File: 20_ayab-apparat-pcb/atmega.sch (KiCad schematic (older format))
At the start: 35 parts, among them P7 CONN_3X2, P8 CONN_4, P9 CONN_2, SW1 SW_PUSH, U6 ATMEGA32U4-A, X1 16MHz, X2 USBMINI

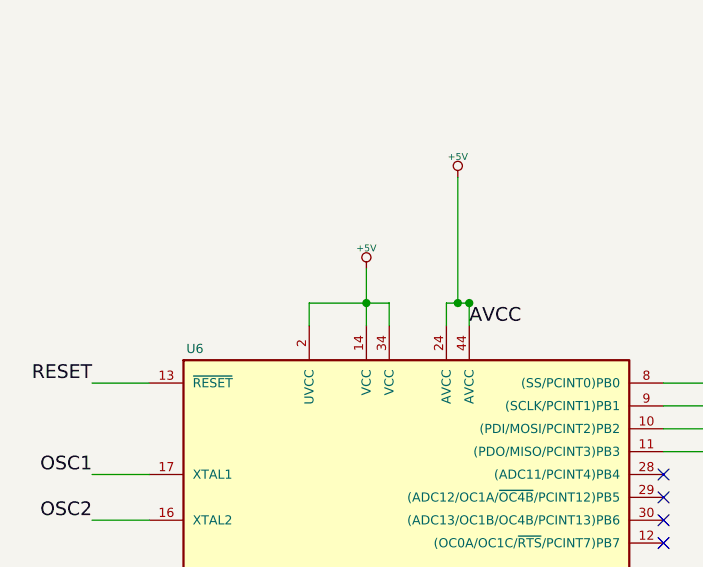
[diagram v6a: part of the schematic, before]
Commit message: Changed power supply of ATMega to VUSB finished BOM CSV -> ready to layout
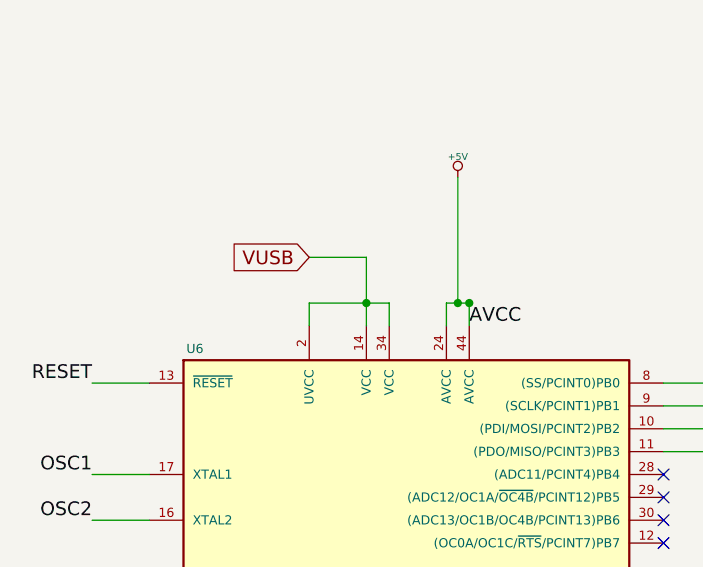
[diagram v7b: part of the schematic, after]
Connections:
- net +5V: no longer U6.14 (VCC), U6.2 (UVCC), U6.34 (VCC)
- net VUSB: now also U6.14 (VCC), U6.2 (UVCC), U6.34 (VCC)
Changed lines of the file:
@@
 $EndComp
 $Comp
-L +5V #PWR037
-U 1 1 52E8098A
-P 2650 2450
-F 0 "#PWR037" H 2650 2540 20  0001 C CNN
-F 1 "+5V" H 2650 2540 30  0000 C CNN
-F 2 "" H 2650 2450 60  0000 C CNN
-F 3 "" H 2650 2450 60  0000 C CNN
-	1    2650 2450
-	1    0    0    -1
-$EndComp
-$Comp
-L PWR_FLAG #FLG038
+L PWR_FLAG #FLG037
 U 1 1 52E809A6
 P 9200 1150
-F 0 "#FLG038" H 9200 1245 30  0001 C CNN
+F 0 "#FLG037" H 9200 1245 30  0001 C CNN
 F 1 "PWR_FLAG" H 9200 1330 30  0000 C CNN
 F 2 "" H 9200 1150 60  0000 C CNN
@@
 $EndComp
 $Comp
-L GND #PWR039
+L GND #PWR038
 U 1 1 52E80AA1
 P 1450 5850
-F 0 "#PWR039" H 1450 5850 30  0001 C CNN
+F 0 "#PWR038" H 1450 5850 30  0001 C CNN
 F 1 "GND" H 1450 5780 30  0001 C CNN
 F 2 "" H 1450 5850 60  0000 C CNN
@@
 ISP
 $Comp
-L GND #PWR040
+L GND #PWR039
 U 1 1 52E80DFA
 P 7100 5850
-F 0 "#PWR040" H 7100 5850 30  0001 C CNN
+F 0 "#PWR039" H 7100 5850 30  0001 C CNN
 F 1 "GND" H 7100 5780 30  0001 C CNN
 F 2 "" H 7100 5850 60  0000 C CNN
@@
 MOSI
 $Comp
-L +5V #PWR041
+L +5V #PWR040
 U 1 1 52E80E45
 P 7100 5600
-F 0 "#PWR041" H 7100 5690 20  0001 C CNN
+F 0 "#PWR040" H 7100 5690 20  0001 C CNN
 F 1 "+5V" H 7100 5690 30  0000 C CNN
 F 2 "" H 7100 5600 60  0000 C CNN
@@
 $EndComp
 $Comp
-L GND #PWR042
+L GND #PWR041
 U 1 1 52E813A7
 P 6750 1800
-F 0 "#PWR042" H 6750 1800 30  0001 C CNN
+F 0 "#PWR041" H 6750 1800 30  0001 C CNN
 F 1 "GND" H 6750 1730 30  0001 C CNN
 F 2 "" H 6750 1800 60  0000 C CNN
@@
 $EndComp
 $Comp
-L +5V #PWR043
+L +5V #PWR042
 U 1 1 52E81906
 P 4350 3500
-F 0 "#PWR043" H 4350 3590 20  0001 C CNN
+F 0 "#PWR042" H 4350 3590 20  0001 C CNN
 F 1 "+5V" H 4350 3590 30  0000 C CNN
 F 2 "" H 4350 3500 60  0000 C CNN
@@
 $EndComp
 $Comp
-L +5V #PWR044
+L +5V #PWR043
 U 1 1 52E81C3C
 P 1300 5300
-F 0 "#PWR044" H 1300 5390 20  0001 C CNN
+F 0 "#PWR043" H 1300 5390 20  0001 C CNN
 F 1 "+5V" H 1300 5390 30  0000 C CNN
 F 2 "" H 1300 5300 60  0000 C CNN
@@
 RESET
 $Comp
-L GND #PWR045
+L GND #PWR044
 U 1 1 52E9637A
 P 2900 6200
-F 0 "#PWR045" H 2900 6200 30  0001 C CNN
+F 0 "#PWR044" H 2900 6200 30  0001 C CNN
 F 1 "GND" H 2900 6130 30  0001 C CNN
 F 2 "" H 2900 6200 60  0000 C CNN
@@
 $EndComp
 $Comp
-L GND #PWR046
+L GND #PWR045
 U 1 1 52E97A05
 P 7150 4350
-F 0 "#PWR046" H 7150 4350 30  0001 C CNN
+F 0 "#PWR045" H 7150 4350 30  0001 C CNN
 F 1 "GND" H 7150 4280 30  0001 C CNN
 F 2 "" H 7150 4350 60  0000 C CNN
@@
 $EndComp
 $Comp
-L GND #PWR047
+L GND #PWR046
 U 1 1 52E97015
 P 10050 1700
-F 0 "#PWR047" H 10050 1700 30  0001 C CNN
+F 0 "#PWR046" H 10050 1700 30  0001 C CNN
 F 1 "GND" H 10050 1630 30  0001 C CNN
 F 2 "" H 10050 1700 60  0000 C CNN
@@
 $EndComp
 $Comp
-L GND #PWR048
+L GND #PWR047
 U 1 1 52E972FE
 P 10550 1700
-F 0 "#PWR048" H 10550 1700 30  0001 C CNN
+F 0 "#PWR047" H 10550 1700 30  0001 C CNN
 F 1 "GND" H 10550 1630 30  0001 C CNN
 F 2 "" H 10550 1700 60  0000 C CNN
@@
 RXLED
 $Comp
-L +5V #PWR049
+L +5V #PWR048
 U 1 1 52E980C3
 P 10050 4500
-F 0 "#PWR049" H 10050 4590 20  0001 C CNN
+F 0 "#PWR048" H 10050 4590 20  0001 C CNN
 F 1 "+5V" H 10050 4590 30  0000 C CNN
 F 2 "" H 10050 4500 60  0000 C CNN
@@
 $EndComp
 $Comp
-L +5V #PWR050
+L +5V #PWR049
 U 1 1 52EA92E6
 P 7750 5650
-F 0 "#PWR050" H 7750 5740 20  0001 C CNN
+F 0 "#PWR049" H 7750 5740 20  0001 C CNN
 F 1 "+5V" H 7750 5740 30  0000 C CNN
 F 2 "" H 7750 5650 60  0000 C CNN
@@
 $EndComp
 $Comp
-L +5V #PWR051
+L +5V #PWR050
 U 1 1 52EA9766
 P 7750 4950
-F 0 "#PWR051" H 7750 5040 20  0001 C CNN
+F 0 "#PWR050" H 7750 5040 20  0001 C CNN
 F 1 "+5V" H 7750 5040 30  0000 C CNN
 F 2 "" H 7750 4950 60  0000 C CNN
@@
 $EndComp
 $Comp
-L GND #PWR052
+L GND #PWR051
 U 1 1 52EA977A
 P 7750 5050
-F 0 "#PWR052" H 7750 5050 30  0001 C CNN
+F 0 "#PWR051" H 7750 5050 30  0001 C CNN
 F 1 "GND" H 7750 4980 30  0001 C CNN
 F 2 "" H 7750 5050 60  0000 C CNN
@@
 LED2
 $Comp
-L +5V #PWR053
+L +5V #PWR052
 U 1 1 52EA9B0A
 P 9150 4500
-F 0 "#PWR053" H 9150 4590 20  0001 C CNN
+F 0 "#PWR052" H 9150 4590 20  0001 C CNN
 F 1 "+5V" H 9150 4590 30  0000 C CNN
 F 2 "" H 9150 4500 60  0000 C CNN
@@
 LED1
 $Comp
-L +5V #PWR054
+L +5V #PWR053
 U 1 1 52EAA0EE
 P 3050 2050
-F 0 "#PWR054" H 3050 2140 20  0001 C CNN
+F 0 "#PWR053" H 3050 2140 20  0001 C CNN
 F 1 "+5V" H 3050 2140 30  0000 C CNN
 F 2 "" H 3050 2050 60  0000 C CNN
@@
 $EndComp
 $Comp
-L +5V #PWR055
+L +5V #PWR054
 U 1 1 52EAA124
 P 8900 1150
-F 0 "#PWR055" H 8900 1240 20  0001 C CNN
+F 0 "#PWR054" H 8900 1240 20  0001 C CNN
 F 1 "+5V" H 8900 1240 30  0000 C CNN
 F 2 "" H 8900 1150 60  0000 C CNN
@@
 NoConn ~ 7900 3200
 $Comp
-L PWR_FLAG #FLG056
+L PWR_FLAG #FLG055
 U 1 1 52EECE74
 P 7800 3350
-F 0 "#FLG056" H 7800 3445 30  0001 C CNN
+F 0 "#FLG055" H 7800 3445 30  0001 C CNN
 F 1 "PWR_FLAG" H 7800 3530 30  0000 C CNN
 F 2 "" H 7800 3350 60  0000 C CNN
@@
 Connection ~ 2800 6150
 Wire Wire Line
-	2650 2450 2650 2700
+	2650 2400 2650 2700
 Wire Wire Line
 	2750 2600 2750 2700
@@
 	7650 3750 7650 3300
 $Comp
-L GND #PWR057
+L GND #PWR056
 U 1 1 52F17DE8
 P 7650 4350
-F 0 "#PWR057" H 7650 4350 30  0001 C CNN
+F 0 "#PWR056" H 7650 4350 30  0001 C CNN
 F 1 "GND" H 7650 4280 30  0001 C CNN
 F 2 "" H 7650 4350 60  0000 C CNN
@@
 Text Notes 7650 5450 0    60   ~ 0
 optional\nI2C extension
+Text GLabel 2400 2400 0    60   Input ~ 0
+VUSB
+Wire Wire Line
+	2400 2400 2650 2400
 $EndSCHEMATC
